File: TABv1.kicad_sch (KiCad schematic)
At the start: 41 parts, among them J10 Conn_02x03_Odd_Even, J11 Conn_02x06_Counter_Clockwise, J5 Conn_02x06_Counter_Clockwise, J6 Conn_02x06_Counter_Clockwise, J9 Conn_02x03_Odd_Even, Q3 DMN2040U, SW2 RESET, U1 RP2350B-QFN80, Y1 12MHz

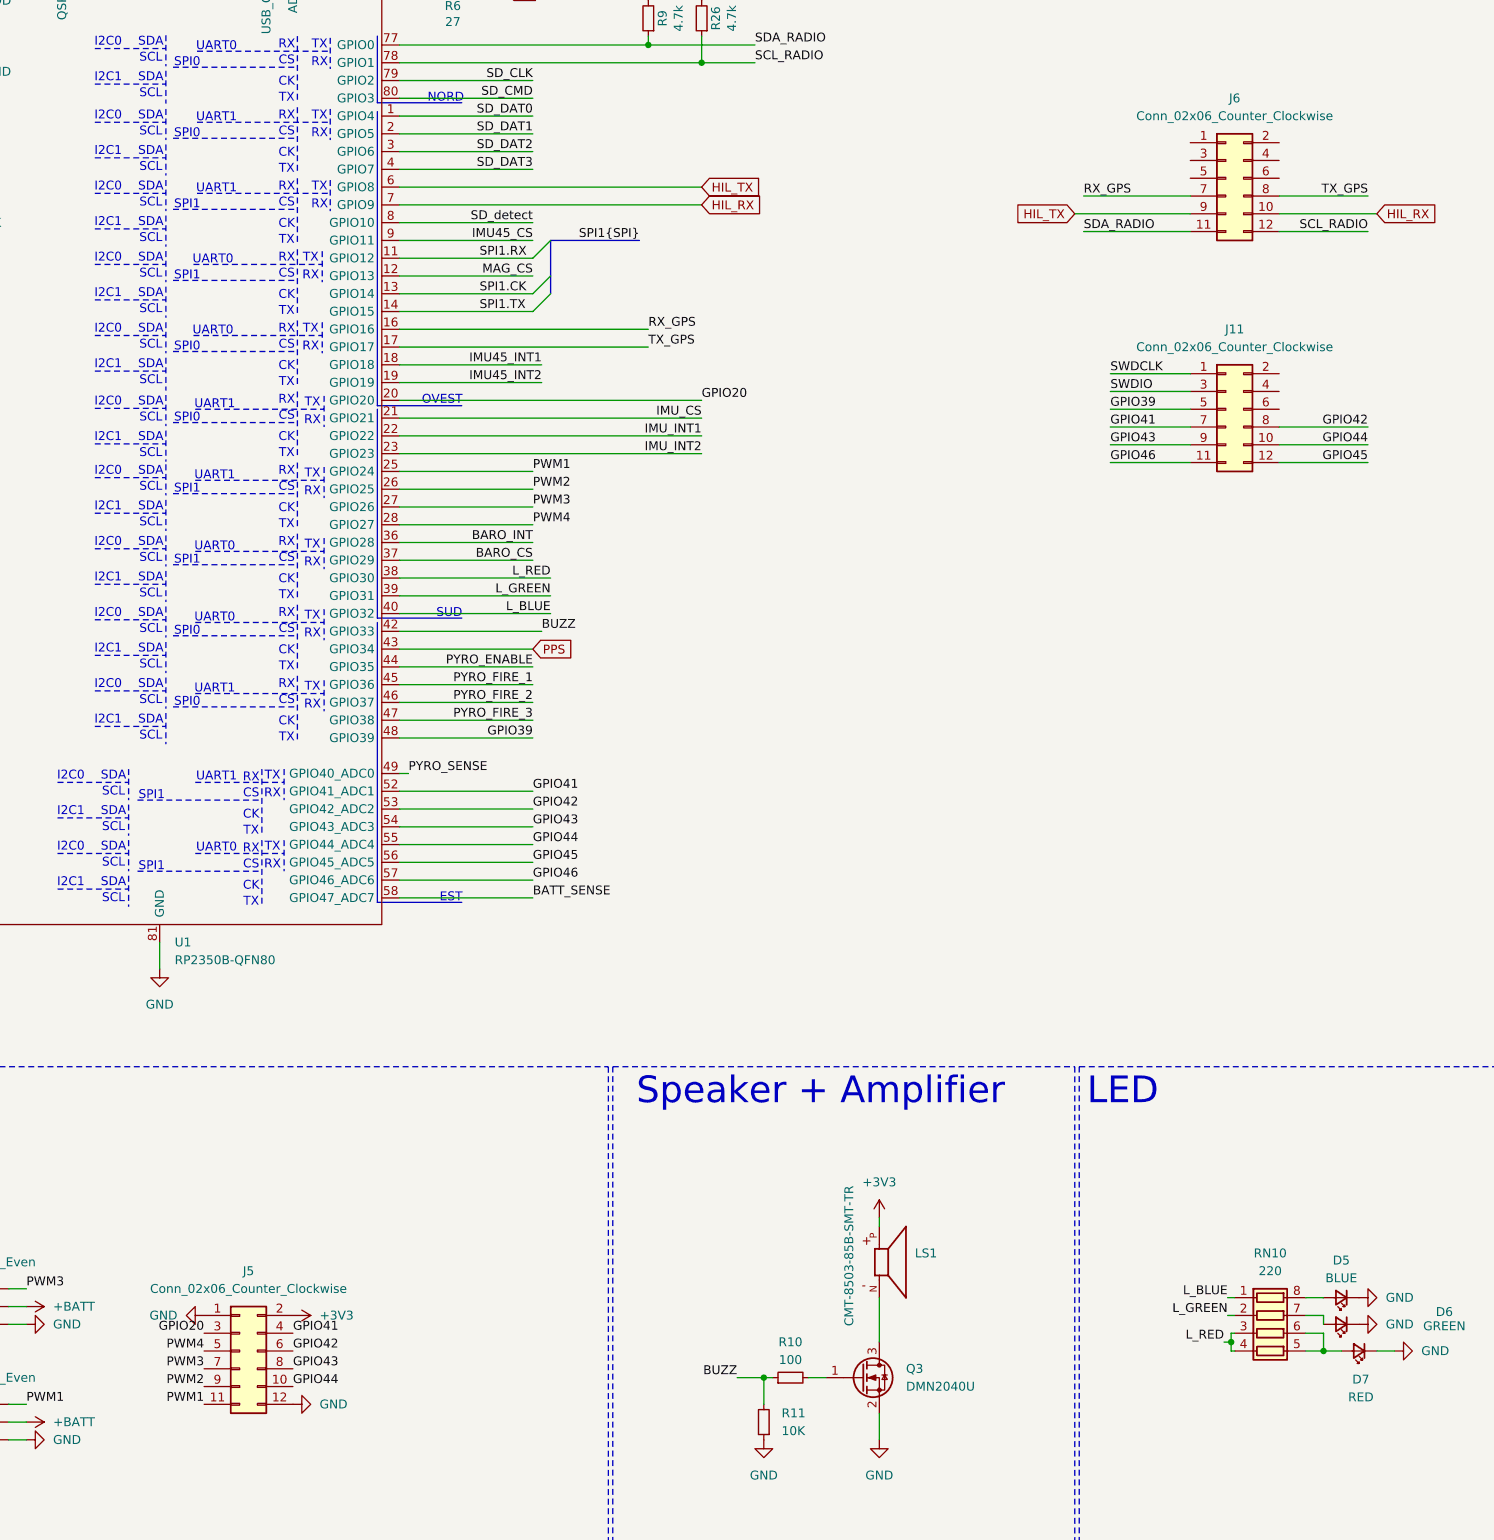
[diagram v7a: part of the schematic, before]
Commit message: connessione 1v1 sotto il rp2350 come la fa raspberry pi, tracce con l impedenza corretta sulla usb, aggiunto collegamenti mancanti e un pò di drc
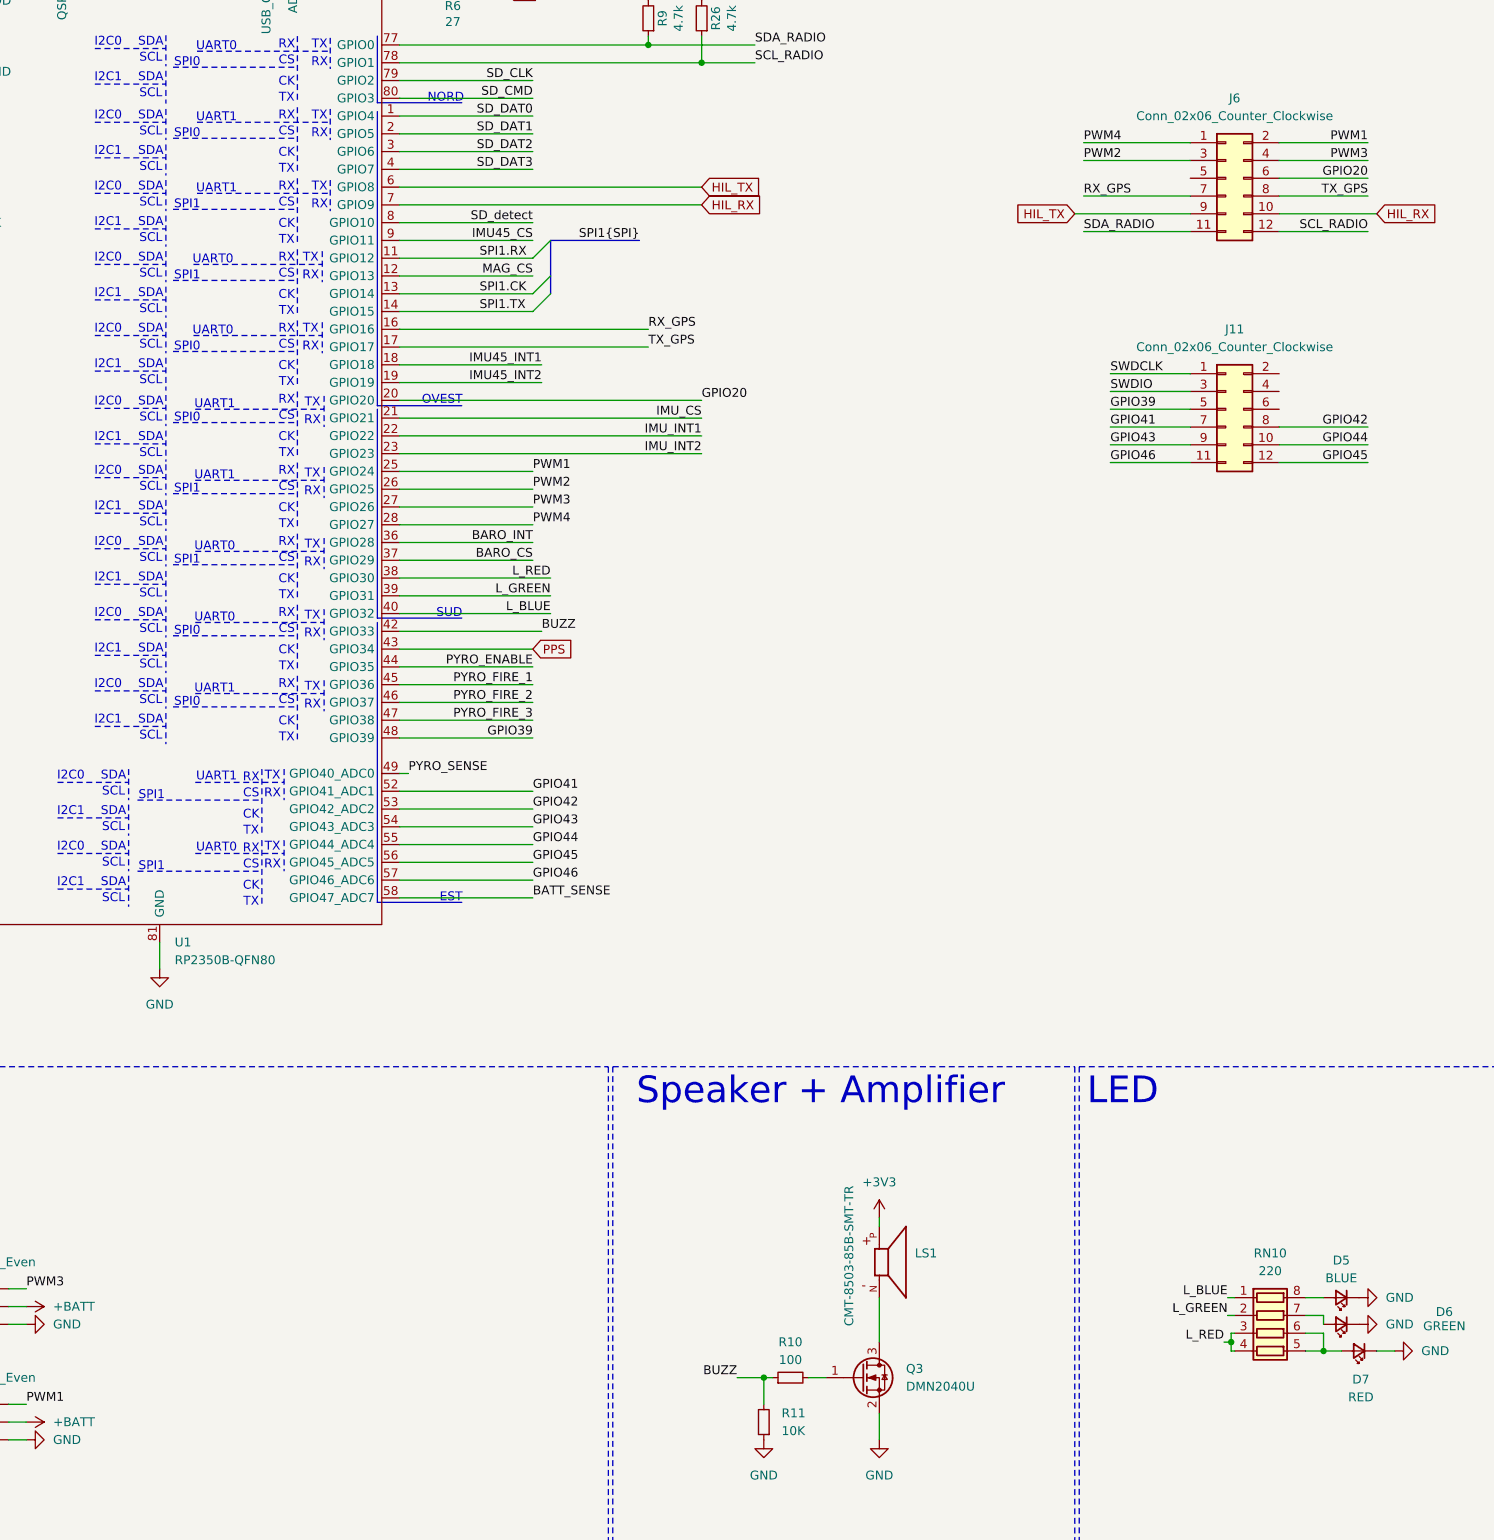
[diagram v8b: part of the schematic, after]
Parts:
- removed J5: Conn_02x06_Counter_Clockwise, Connector_PinHeader_2.54mm:PinHeader_2x06_P2.54mm_Vertical, symbol Connector_Generic:Conn_02x06_Odd_Even
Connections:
- net GPIO20: now also J6.6 (Pin_6)
- net PWM1: now also J6.2 (Pin_2)
- net PWM2: now also J6.3 (Pin_3)
- net PWM3: now also J6.4 (Pin_4)
- net PWM4: now also J6.1 (Pin_1)
